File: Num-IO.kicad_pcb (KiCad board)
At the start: 2 copper layers, 170.2 x 61.1 mm, 127 parts, among them J1 DB37_Female, J2 DB37_Male, J3 Conn_02x25_Odd_Even, J4 0826-1X1T-GH-F, J5 Conn_01x02_Male, J6 Conn_01x02_Male, J7 Conn_01x02_Male, J8 Conn_01x02_Male, J9 Conn_01x02_Male, U1 MAX14917AFM+, U10 LTC6820HMS, U11 LTC6820HMS, U12 LTC6820HMS, U13 AP1117-33, U2 MAX14917AFM+, U3 MAX14851AEE+, U4 MAX14917AFM+, U5 MAX31910AUI+, U6 MAX31910AUI+, U7 MAX31910AUI+, U8 MAX31910AUI+, U9 LTC6820HMS

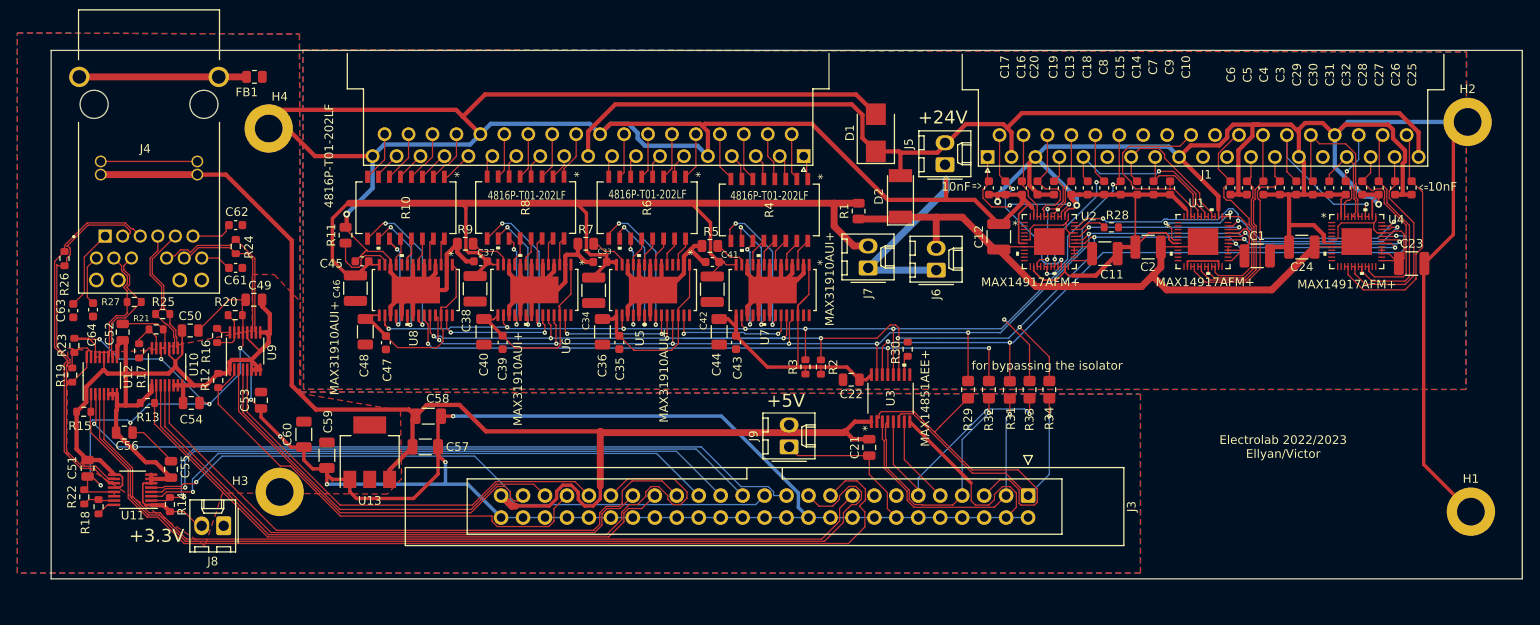
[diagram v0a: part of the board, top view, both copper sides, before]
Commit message: add MPGA and MPGB on a DB25 (isolated)
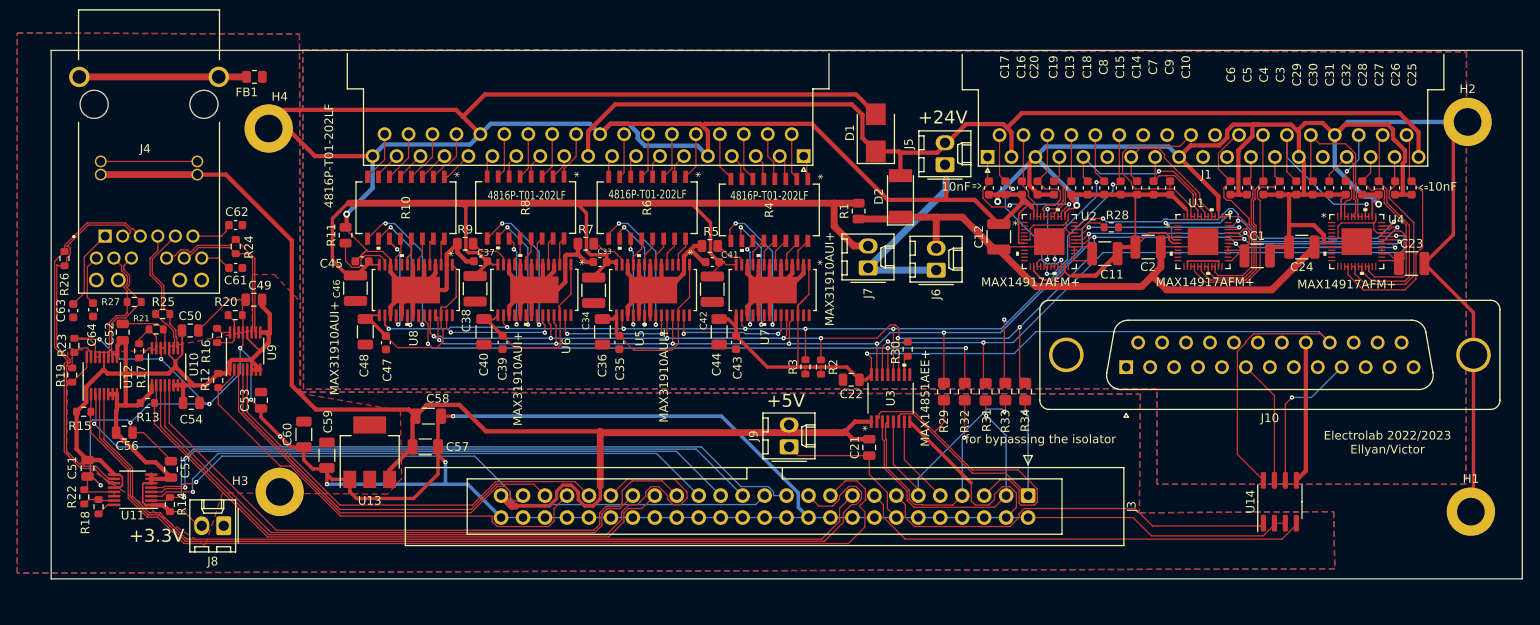
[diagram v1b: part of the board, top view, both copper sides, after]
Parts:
- added J10: DB25_Female, Connector_Dsub:DSUB-25_Female_Vertical_P2.77x2.84mm_MountingHoles, F.Cu at (184.2, 60.9)
- added U14: HCPL-063A, Package_SO:SOIC-8_3.9x4.9mm_P1.27mm, F.Cu at (201.9, 76.5)
- moved R32 2.80 mm to (165.5, 63.7)
- moved R29 2.80 mm to (163.1, 63.7)
- moved R31 2.80 mm to (167.9, 63.7)
- moved R33 2.80 mm to (170.2, 63.7)
- moved R34 2.80 mm to (172.5, 63.7)
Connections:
- J3 pad 13: /FPGA Connector/MPGA -> /IMPGA
- J3 pad 15: /FPGA Connector/MPGB -> /IMPGB
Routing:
- net /IsoPWR: track 38.7 -> 124.7 mm, vias 0 -> 1
- net /IMPGB: track 0.00 -> 52.6 mm
- net /IMPGA: track 0.00 -> 46.9 mm
- net GNDD: track 326.5 -> 357.9 mm
- net /MPGB: track 0.00 -> 17.1 mm, vias 0 -> 1
- net GNDPWR: track 667.8 -> 684.4 mm
- net /MPGA: track 0.00 -> 14.5 mm
- net /I*FAULT: track 30.0 -> 26.5 mm
- net /SDO: track 75.5 -> 73.1 mm
- net /FPGA Connector/SPI0.SDO: track 29.6 -> 28.2 mm
- net /FPGA Connector/SPI0.CLK: track 39.9 -> 38.5 mm
- net /FPGA Connector/SPI0.*CS: track 31.9 -> 30.8 mm
- net /CS: track 150.6 -> 149.7 mm
- net /*FAULT: track 157.7 -> 156.8 mm
- net /FPGA Connector/SPI0.SDI: track 34.0 -> 34.6 mm

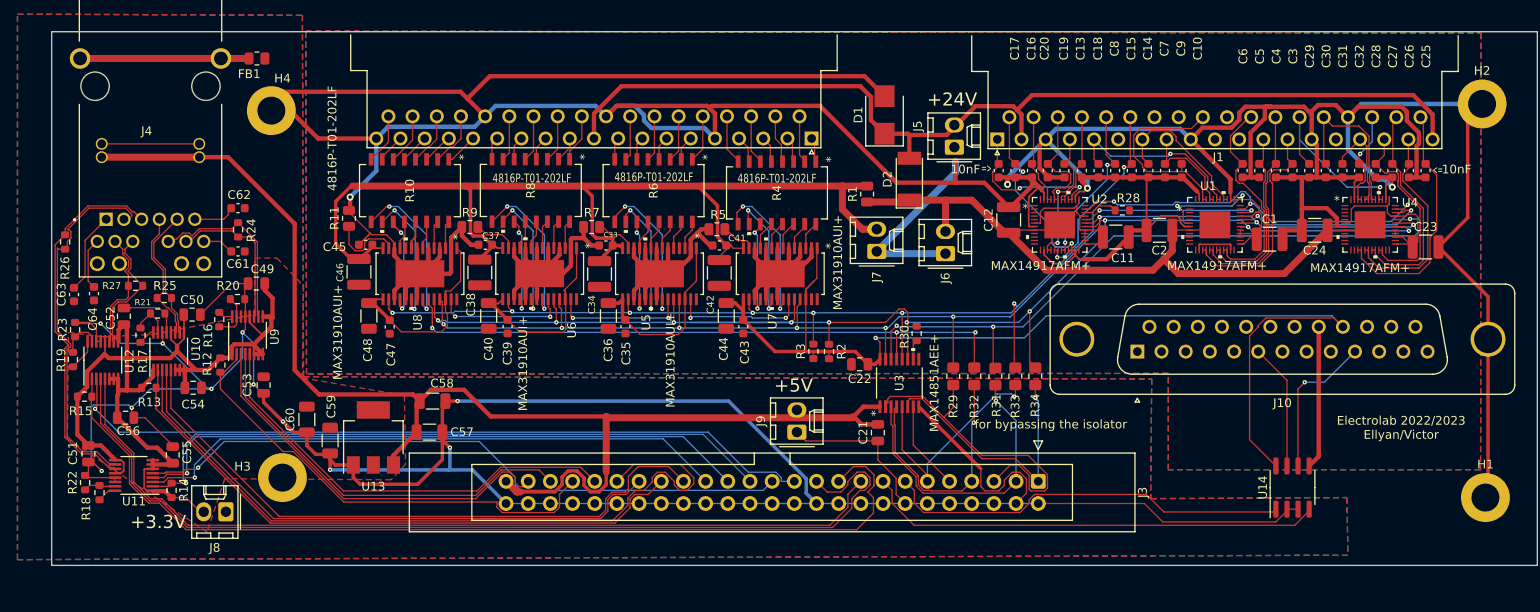
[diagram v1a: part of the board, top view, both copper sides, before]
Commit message: add condo for MPG isolator + small rerouting pair diff
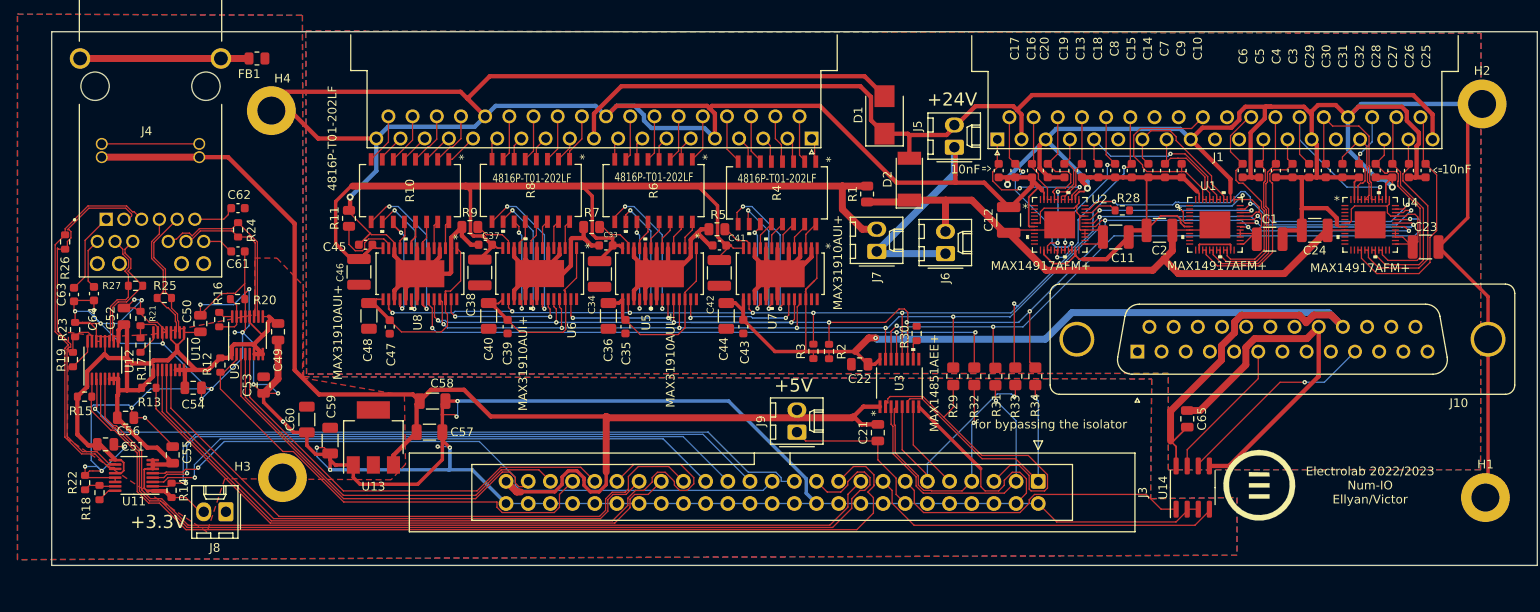
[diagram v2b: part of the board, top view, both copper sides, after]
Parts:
- added C65: 0.1uF, Capacitor_SMD:C_0805_2012Metric, F.Cu at (189.9, 68.6)
- added G***: LOGO, logo:electrologo, F.Cu at (198.1, 76.2)
- moved U14 11.4 mm to (190.5, 76.5)
- moved C49 6.05 mm to (85.7, 58.6), turned to -90 degrees
- moved C51 2.24 mm to (66.0, 71.5), turned to 0 degrees
- moved R21 2.05 mm to (70.0, 57.1), turned to 90 degrees
- moved C50 1.40 mm to (76.8, 57.7), turned to 90 degrees
- moved R17 1.14 mm to (70.0, 60.1)
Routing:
- net GNDD: track 357.9 -> 415.6 mm, vias 11 -> 26
- net GNDPWR: track 684.4 -> 713.9 mm
- net /IMPGA: track 46.9 -> 35.2 mm
- net /IMPGB: track 52.6 -> 41.2 mm
- net /IsoPWR: track 124.7 -> 133.7 mm
- net /MPGB: track 17.1 -> 23.5 mm
- net +3V3: track 109.8 -> 106.7 mm
- net /MPGA: track 14.5 -> 16.5 mm
- net Net-(R17-Pad2): track 1.96 -> 2.89 mm
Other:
- board text added: "Electrolab 2022/2023 Num-IO Ellyan/Victor"
- board text removed: "Electrolab 2022/2023 Ellyan/Victor"

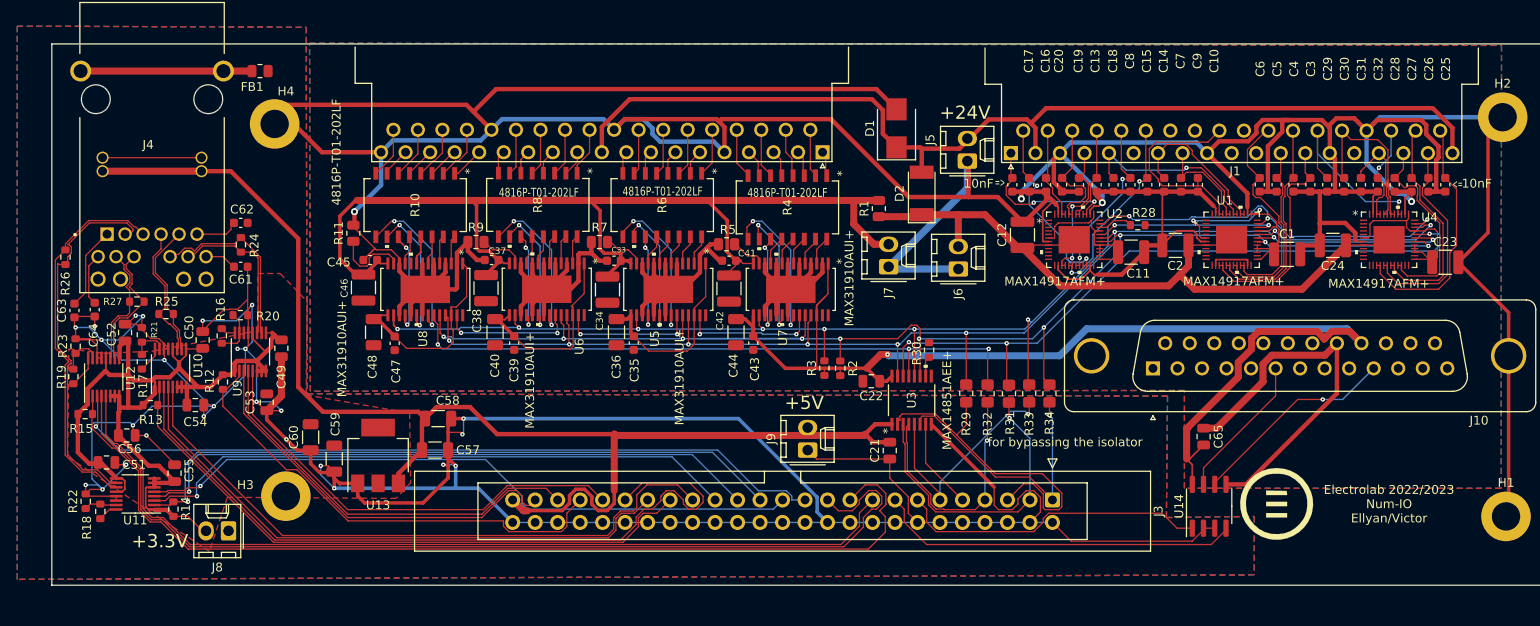
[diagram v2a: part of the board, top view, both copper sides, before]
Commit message: add vias
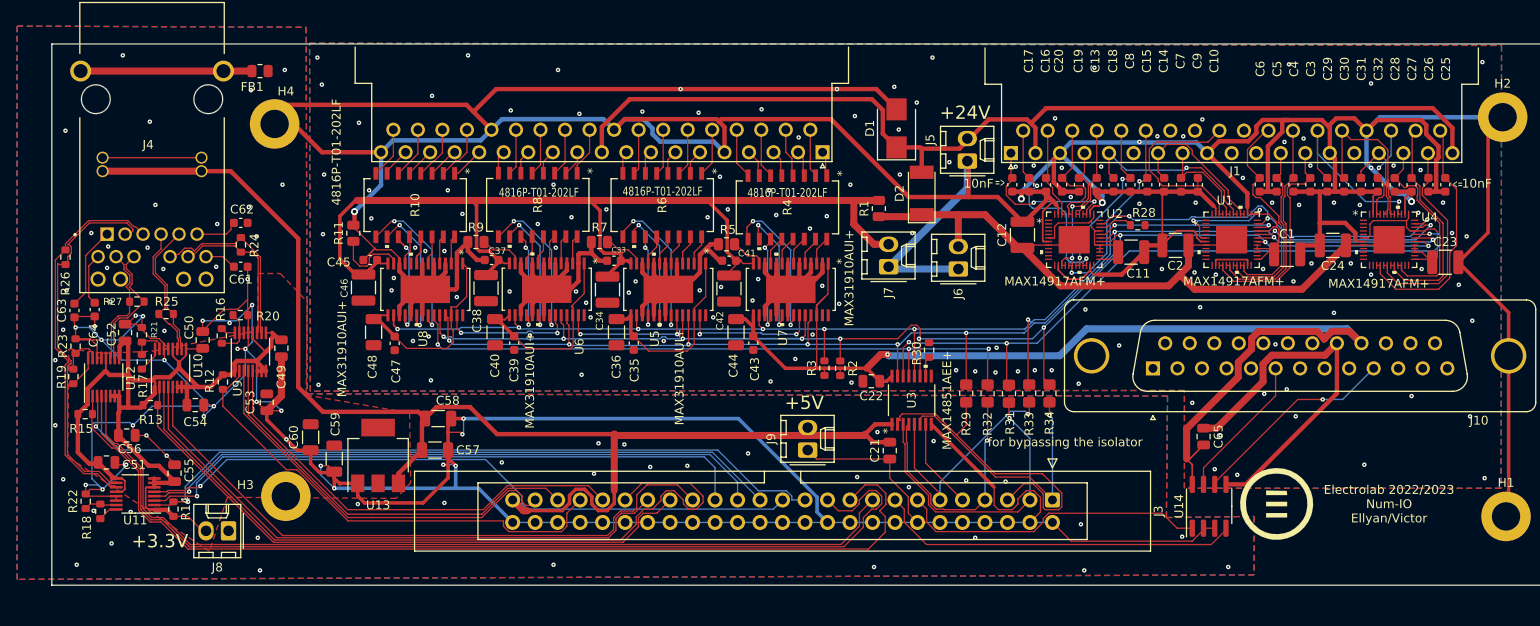
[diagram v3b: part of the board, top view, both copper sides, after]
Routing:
- net /FPGA Connector/SPI2.SDO: track 68.3 -> 70.5 mm
- net /output channel 17-24/OUT4: track 21.0 -> 22.9 mm
- net /FPGA Connector/SPI2.SDI: track 76.0 -> 74.6 mm
- net /CLK: track 146.5 -> 147.3 mm
- net /*FAULT: track 156.8 -> 157.5 mm
- net /output channel 17-24/OUT2: track 21.6 -> 22.2 mm
- net GNDPWR: vias 4 -> 141
- net GNDD: vias 26 -> 80

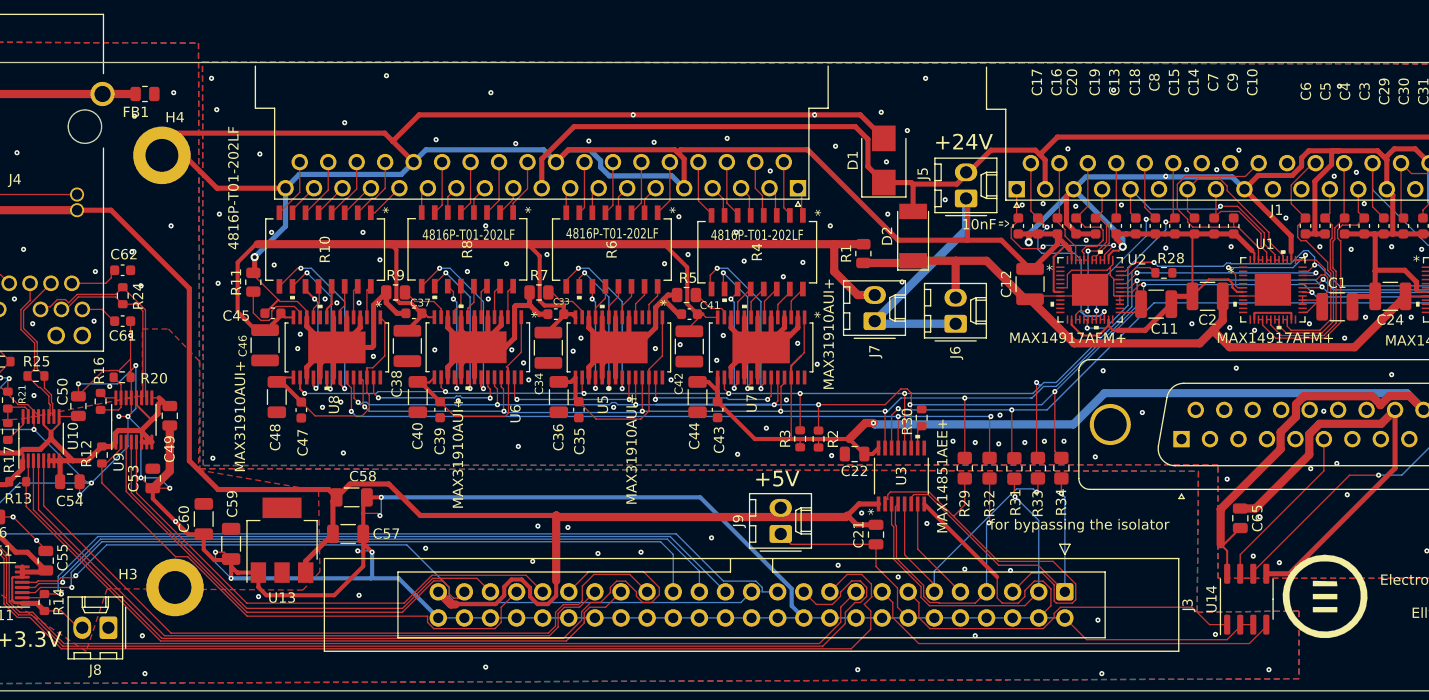
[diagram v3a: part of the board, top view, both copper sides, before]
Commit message: add zeners in the meantime, if the SPI isolator is delayed
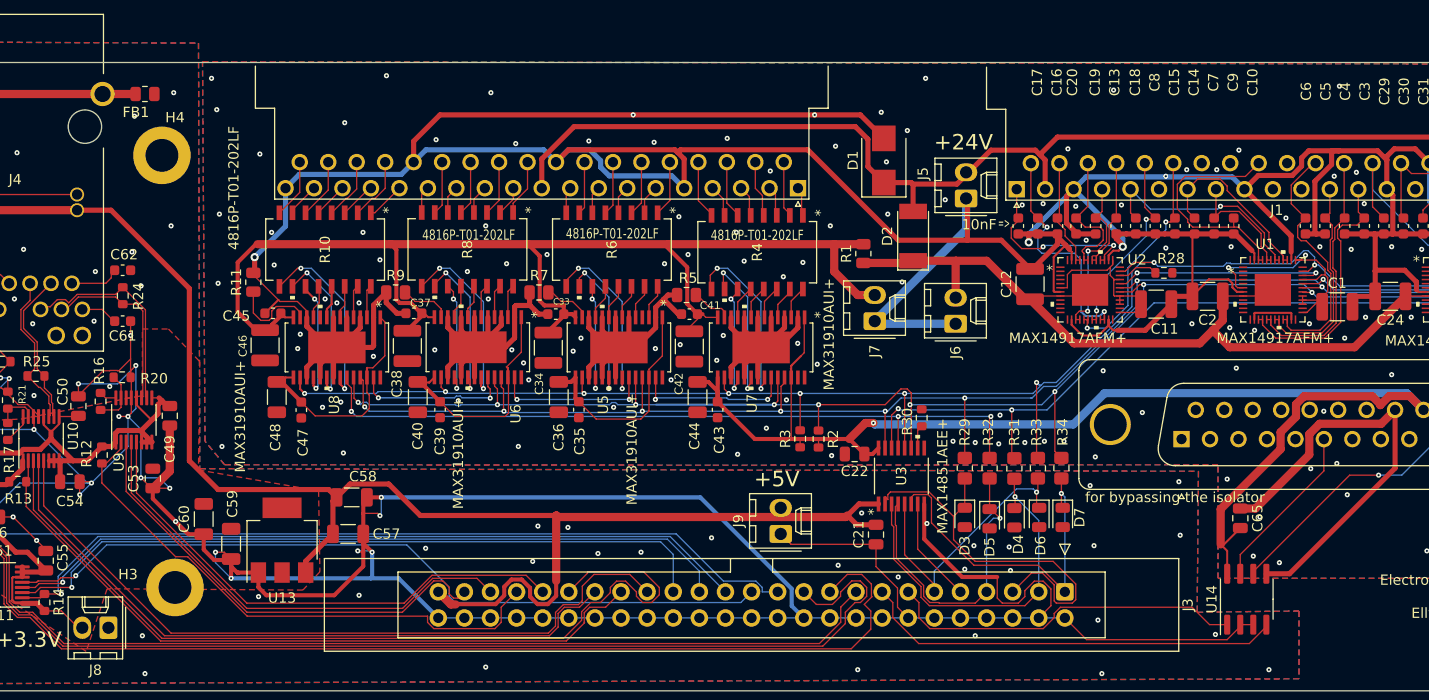
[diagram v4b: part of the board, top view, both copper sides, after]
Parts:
- removed G***: LOGO, logo:electrologo
- added D3: BZY55B5V6 RBG, Diode_SMD:D_0805_2012Metric, F.Cu at (163.1, 68.5)
- added D4: BZY55B5V6 RBG, Diode_SMD:D_0805_2012Metric, F.Cu at (167.9, 68.5)
- added D5: BZY55B5V6 RBG, Diode_SMD:D_0805_2012Metric, F.Cu at (165.5, 68.6)
- added D6: BZY55B5V6 RBG, Diode_SMD:D_0805_2012Metric, F.Cu at (170.3, 68.5)
- added D7: BZY55B5V6 RBG, Diode_SMD:D_0805_2012Metric, F.Cu at (172.6, 68.5)
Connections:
- H4 pad 1: GNDPWR -> (no net)
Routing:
- net GNDPWR: track 713.9 -> 674.0 mm
- net /FPGA Connector/SPI0.*CS: track 30.8 -> 33.7 mm
- net GNDD: track 415.6 -> 417.6 mm, vias 80 -> 86
- net /I*FAULT: track 26.5 -> 28.2 mm
- net /FPGA Connector/SPI0.CLK: track 38.5 -> 39.8 mm
- net /FPGA Connector/SPI0.SDO: track 28.2 -> 29.4 mm
- net /FPGA Connector/SPI0.SDI: track 34.6 -> 35.7 mm
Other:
- copper layers 2 -> 4
